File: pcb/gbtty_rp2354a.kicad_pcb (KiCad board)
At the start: 2 copper layers, 63.5 x 26 mm, 37 parts, among them J1 USB_C_Receptacle_USB2.0_16P, J2 SM03B-SRSS-TB, J3 GameBoy_LinkPort, SW1 SW_Push, U2 NCP1117-3.3_SOT223, U3 RP2354A, U4 ADG3304, Y1 ABM8-272-T3

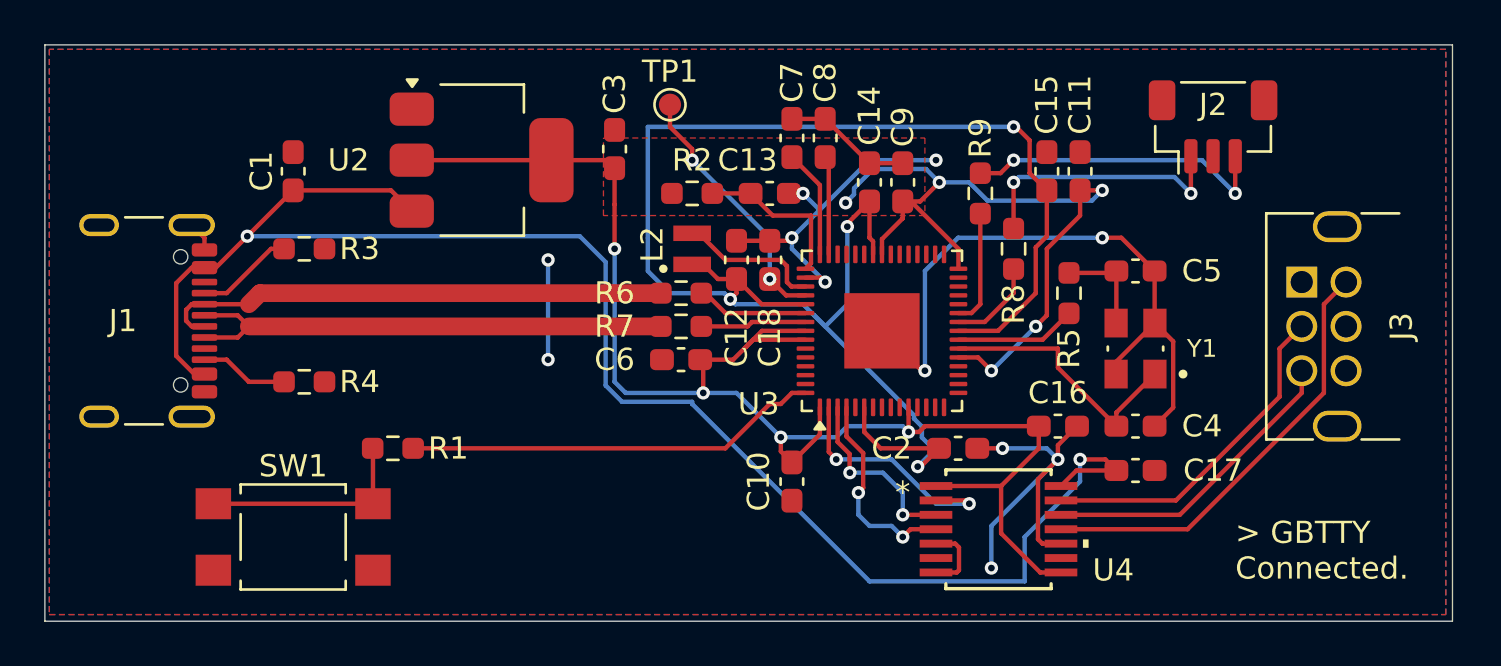
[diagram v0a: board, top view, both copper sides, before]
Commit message: pcb: Put the rp2354a design in the shrink-ray
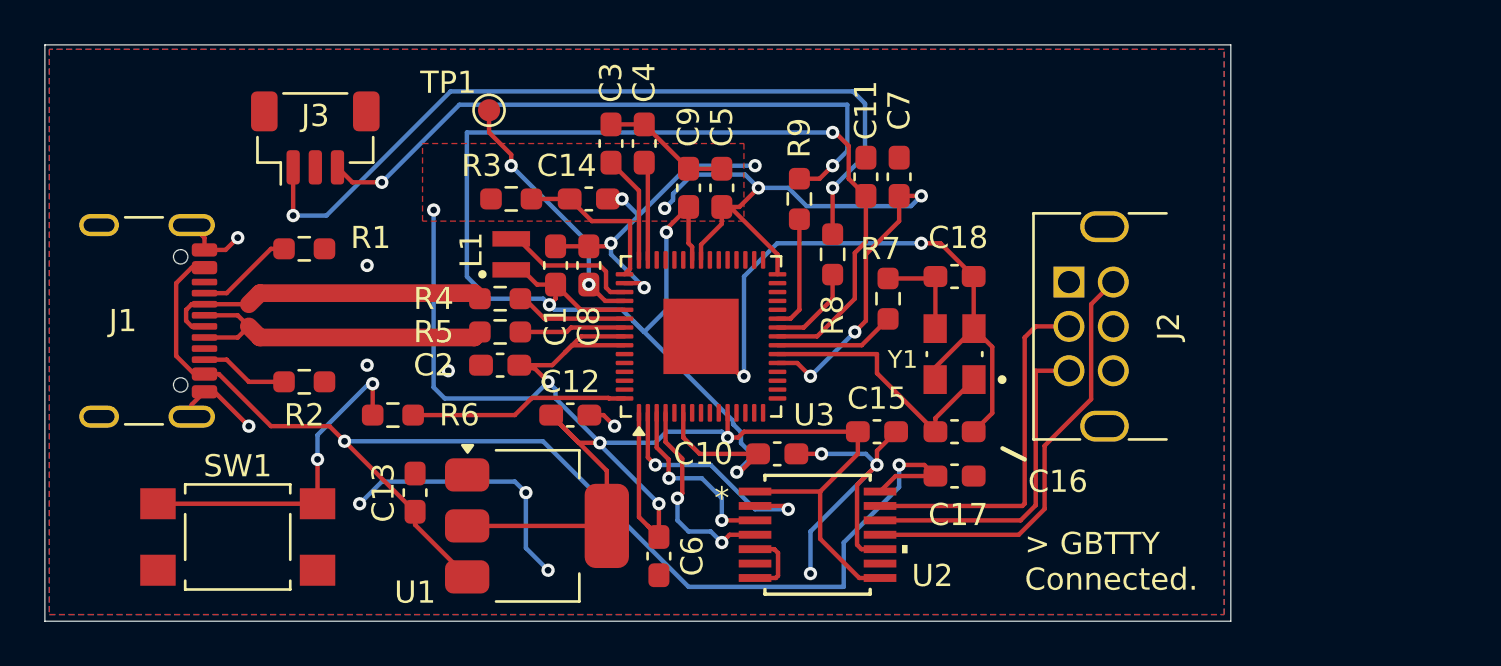
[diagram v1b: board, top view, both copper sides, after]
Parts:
- moved J3 40.5 mm to (120.0, 88.0)
- moved U1 16.7 mm to (130.0, 105.5)
- moved C13 15.5 mm to (124.5, 104.0)
- moved C12 12.2 mm to (131.5, 100.5), turned to 0 degrees
- moved J2 10.5 mm to (154.0, 94.5)
- moved C1 8.17 mm to (130.8, 93.8)
- moved C10 8.17 mm to (140.8, 102.2)
- moved C11 8.17 mm to (144.8, 89.8)
- moved C14 8.17 mm to (132.3, 90.8)
- moved C15 8.17 mm to (145.3, 101.2)
- moved C16 8.17 mm to (148.8, 101.2)
- moved C17 8.17 mm to (148.8, 103.2)
- moved C18 8.17 mm to (148.8, 94.2)
- moved C2 8.17 mm to (128.3, 98.2)
- moved C3 8.17 mm to (133.3, 88.2)
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- renumbered C12 to C1, C2 to C10, C15 to C11, C3 to C12, C1 to C13, C13 to C14, C16 to C15, C4 to C16, C5 to C18, C6 to C2, C7 to C3, C8 to C4, C9 to C5, C10 to C6, C11 to C7, C18 to C8, C14 to C9, J3 to J2, J2 to J3, L2 to L1, R3 to R1, R4 to R2, R2 to R3, R6 to R4, R7 to R5, R1 to R6, R5 to R7, U2 to U1, U4 to U2
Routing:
- net Net-(J3-Pin_1): track 12.2 -> 37.0 mm
- net Net-(J3-Pin_3): track 14.0 -> 29.5 mm
- net VBUS: track 73.7 -> 58.9 mm
- net GND: track 77.3 -> 91.9 mm, vias 11 -> 18
- net +3V3: track 122.5 -> 135.1 mm, vias 11 -> 12
- net Net-(U3-~{QSPI_SS}): track 18.7 -> 9.87 mm
- net D-: track 23.2 -> 15.1 mm
- net D+: track 23.0 -> 15.1 mm
- net Net-(R6-Pad1): track 9.71 -> 15.2 mm, vias 0 -> 2
- net Net-(J2-SI): track 15.4 -> 16.3 mm
- net Net-(J2-SC): track 14.1 -> 14.9 mm
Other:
- board size 63.5 x 26 mm -> 53.5 x 26 mm
